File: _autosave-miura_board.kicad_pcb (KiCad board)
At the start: 2 copper layers, 60 x 60 mm, 41 parts, among them J1 Screw_Terminal_01x02, J2 Screw_Terminal_01x02, J3 Screw_Terminal_01x02, J4 Conn_01x04_Male, J5 Screw_Terminal_01x02, J6 Screw_Terminal_01x02, J7 Screw_Terminal_01x02, J8 Screw_Terminal_01x02, SW1 SW_Push, SW2 SW_Push, U1 ESP32-WROOM, U2 W25Q32JVSS, U3 DRV8833PW, U4 DRV8833PW, U5 AMS1117, U6 MPU-6050, U7 L7806, U8 DRV8833PW

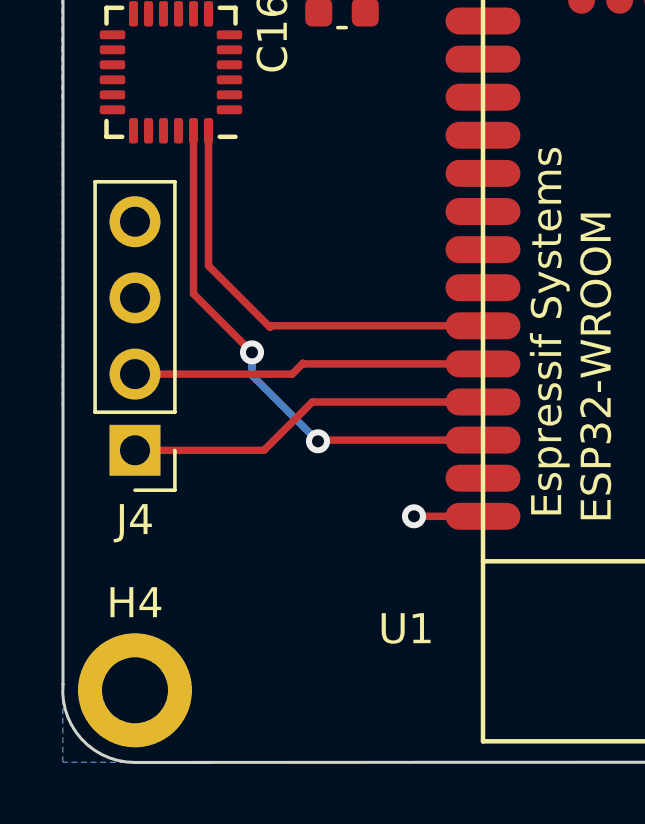
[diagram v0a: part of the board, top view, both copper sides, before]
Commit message: Verify sch and begin route
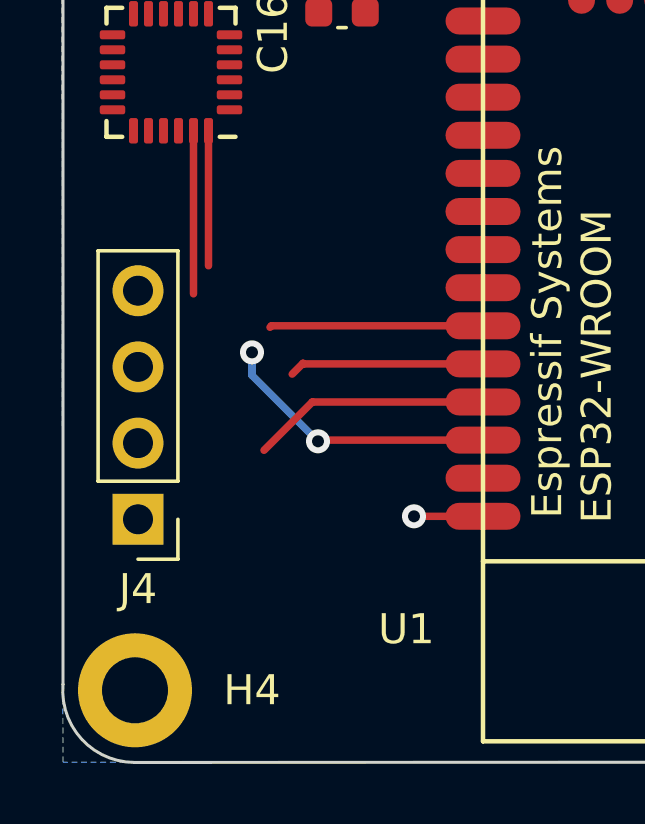
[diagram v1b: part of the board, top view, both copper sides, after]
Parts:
- moved J4 2.30 mm to (63.5, 76.8)
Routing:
- net RXD0: track 11.8 -> 6.52 mm
- net TXD0: track 12.3 -> 7.97 mm
- net SDA: track 14.5 -> 11.6 mm
- net SCL: track 17.6 -> 14.8 mm
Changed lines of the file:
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@@
     (property "Sheetname" "")
     (attr exclude_from_pos_files)
-    (fp_text reference "H4" (at 0 -2.9) (layer "F.SilkS")
+    (fp_text reference "H4" (at 3.9 0) (layer "F.SilkS")
       (effects (font (size 1 1) (thickness 0.15)))
     )
@@
   )
   (footprint "Connector_PinHeader_2.54mm:PinHeader_1x04_P2.54mm_Vertical" (layer "F.Cu")
-    (at 63.4 74.5 180)
+    (at 63.5 76.8 180)
     (descr "Through hole straight pin header, 1x04, 2.54mm pitch, single row")
     (tags "Through hole pin header THT 1x04 2.54mm single row")
@@
   (segment (start 109.1 32.55) (end 109.1 38.85) (width 0.8) (layer "F.Cu") (net 15))
   (segment (start 69.31 72.89) (end 75 72.89) (width 0.25) (layer "F.Cu") (net 24))
-  (segment (start 63.4 74.5) (end 67.7 74.5) (width 0.25) (layer "F.Cu") (net 24))
   (segment (start 67.7 74.5) (end 69.31 72.89) (width 0.25) (layer "F.Cu") (net 24))
   (segment (start 69 71.6) (end 69.02 71.62) (width 0.25) (layer "F.Cu") (net 27))
   (segment (start 68.64 71.96) (end 69 71.6) (width 0.25) (layer "F.Cu") (net 27))
   (segment (start 69.02 71.62) (end 75 71.62) (width 0.25) (layer "F.Cu") (net 27))
-  (segment (start 63.4 71.96) (end 68.64 71.96) (width 0.25) (layer "F.Cu") (net 27))
   (segment (start 79.675 45.625) (end 79.7 45.6) (width 0.25) (layer "F.Cu") (net 30))
   (segment (start 98.72 42.2) (end 91.675 42.2) (width 0.8) (layer "F.Cu") (net 30))
   (segment (start 91.675 42.2) (end 91.6 42.125) (width 0.8) (layer "F.Cu") (net 30))
   (segment (start 79.6625 45.625) (end 79.675 45.625) (width 0.25) (layer "F.Cu") (net 30))
-  (segment (start 65.85 68.35) (end 67.9 70.4) (width 0.25) (layer "F.Cu") (net 62))
   (segment (start 67.95 70.35) (end 75 70.35) (width 0.25) (layer "F.Cu") (net 62))
   (segment (start 65.85 63.85) (end 65.85 68.35) (width 0.25) (layer "F.Cu") (net 62))
@@
   (segment (start 69.5 74.2) (end 69.54 74.16) (width 0.25) (layer "F.Cu") (net 63))
   (segment (start 69.54 74.16) (end 75 74.16) (width 0.25) (layer "F.Cu") (net 63))
-  (segment (start 65.35 69.2855) (end 67.3 71.2355) (width 0.25) (layer "F.Cu") (net 63))
   (segment (start 65.35 63.85) (end 65.35 69.2855) (width 0.25) (layer "F.Cu") (net 63))
   (via (at 69.5 74.2) (size 0.8) (drill 0.4) (layers "F.Cu" "B.Cu") (net 63))

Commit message: lol
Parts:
- moved U2 19.1 mm to (100.7, 62.0), turned to 0 degrees
- moved U8 9.33 mm to (86.1, 46.1)
- moved C15 7.69 mm to (63.1, 62.6), turned to 90 degrees
- moved U6 4.26 mm to (67.9, 64.6)
- moved C16 2.04 mm to (66.2, 60.2)
- moved R1 1.91 mm to (106.5, 75.0)
- moved C7 1.90 mm to (106.5, 71.4)
- moved J4 1.20 mm to (63.5, 78.0)
- moved U3 0.14 mm to (76.6, 37.7)
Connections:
- J6 pad 2: Net-(J6-Pad2) -> Net-(U3-Pad2)
- U1 pad 10: MOTOR_B12_IN -> MOTOR_A31_IN
- U1 pad 11: MOTOR_B11_IN -> MOTOR_A32_IN
- U1 pad 12: MOTOR_A12_IN -> MOTOR_B31_IN
- U1 pad 13: MOTOR_A11_IN -> MOTOR_B32_IN
- U1 pad 14: unconnected-(U1-Pad14) -> MOTOR_B11_IN
- U1 pad 16: unconnected-(U1-Pad16) -> MOTOR_B12_IN
- U1 pad 23: unconnected-(U1-Pad23) -> MOTOR_A12_IN
- U1 pad 24: unconnected-(U1-Pad24) -> MOTOR_A11_IN
- U1 pad 6: MOTOR_B22_IN -> MOTOR_A21_IN
- U1 pad 7: MOTOR_B21_IN -> MOTOR_A22_IN
- U1 pad 8: MOTOR_A22_IN -> MOTOR_B22_IN
- U1 pad 9: MOTOR_A21_IN -> MOTOR_B21_IN
- U3 pad 2: Net-(J6-Pad1) -> Net-(U3-Pad2)
- U3 pad 4: Net-(J6-Pad2) -> Net-(J6-Pad1)
- U3 pad 5: Net-(J2-Pad2) -> Net-(J2-Pad1)
- U3 pad 7: Net-(J2-Pad1) -> Net-(J2-Pad2)
- U8 pad 10: MOTOR_B22_IN -> MOTOR_B32_IN
- U8 pad 15: MOTOR_A22_IN -> MOTOR_A32_IN
- U8 pad 16: MOTOR_A21_IN -> MOTOR_A31_IN
- U8 pad 9: MOTOR_B21_IN -> MOTOR_B31_IN
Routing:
- net MOTOR_SUPPLY: track 7.20 -> 68.7 mm
- net GND: track 44.6 -> 88.7 mm, vias 14 -> 29
- net MOTOR_B11_IN: track 0.00 -> 31.6 mm
- net MOTOR_B12_IN: track 0.00 -> 29.6 mm
- net MOTOR_A11_IN: track 0.00 -> 27.5 mm
- net MOTOR_A12_IN: track 0.00 -> 26.5 mm
- net MOTOR_B21_IN: track 0.00 -> 20.0 mm, vias 0 -> 2
- net MOTOR_A21_IN: track 0.00 -> 19.7 mm, vias 0 -> 2
- net MOTOR_A22_IN: track 0.00 -> 19.6 mm, vias 0 -> 2
- net Net-(J1-Pad2): track 0.00 -> 19.2 mm, vias 0 -> 1
- net MOTOR_B22_IN: track 0.00 -> 18.8 mm, vias 0 -> 2
- net +3V3: track 26.9 -> 45.7 mm
- net Net-(J1-Pad1): track 0.00 -> 18.7 mm, vias 0 -> 1
- net Net-(J6-Pad1): track 0.00 -> 17.6 mm
- net Net-(J7-Pad1): track 0.00 -> 17.4 mm
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- added copper zone on F.Cu, net +3V3
